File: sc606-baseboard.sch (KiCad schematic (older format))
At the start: 0 parts

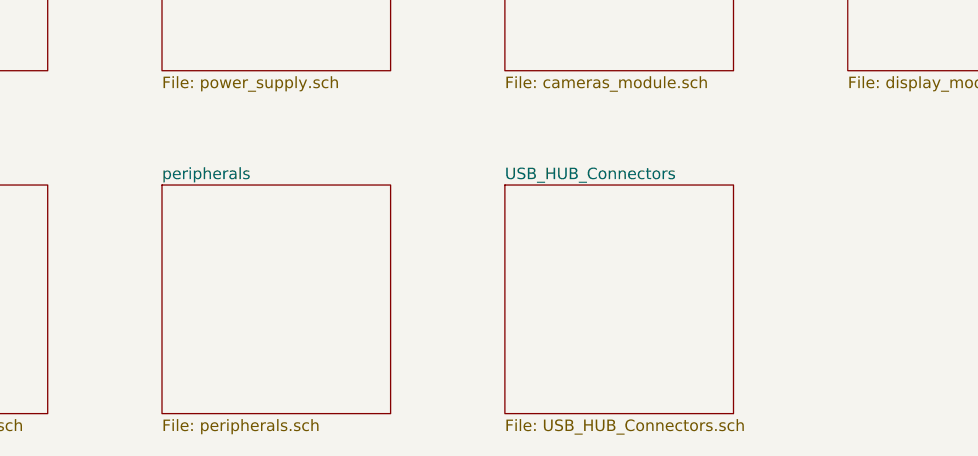
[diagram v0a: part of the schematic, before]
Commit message: Added footprint of 2x USB-A stacked. Added connections to USB HUB.
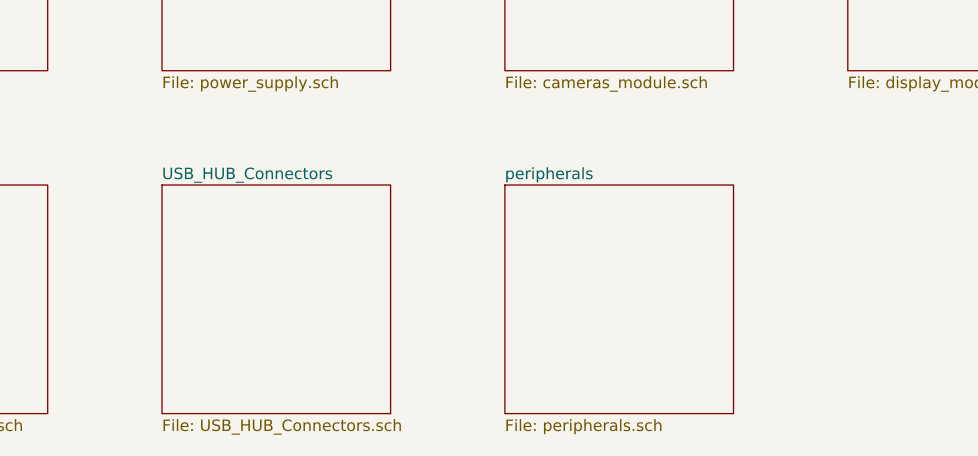
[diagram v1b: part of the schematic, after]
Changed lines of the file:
@@
 $EndSheet
 $Sheet
-S 7000 7500 1000 1000
+S 8500 7500 1000 1000
 U 61D49FDE
 F0 "peripherals" 50
@@
 $EndSheet
 $Sheet
-S 8500 7500 1000 1000
+S 7000 7500 1000 1000
 U 63348E64
 F0 "USB_HUB_Connectors" 50

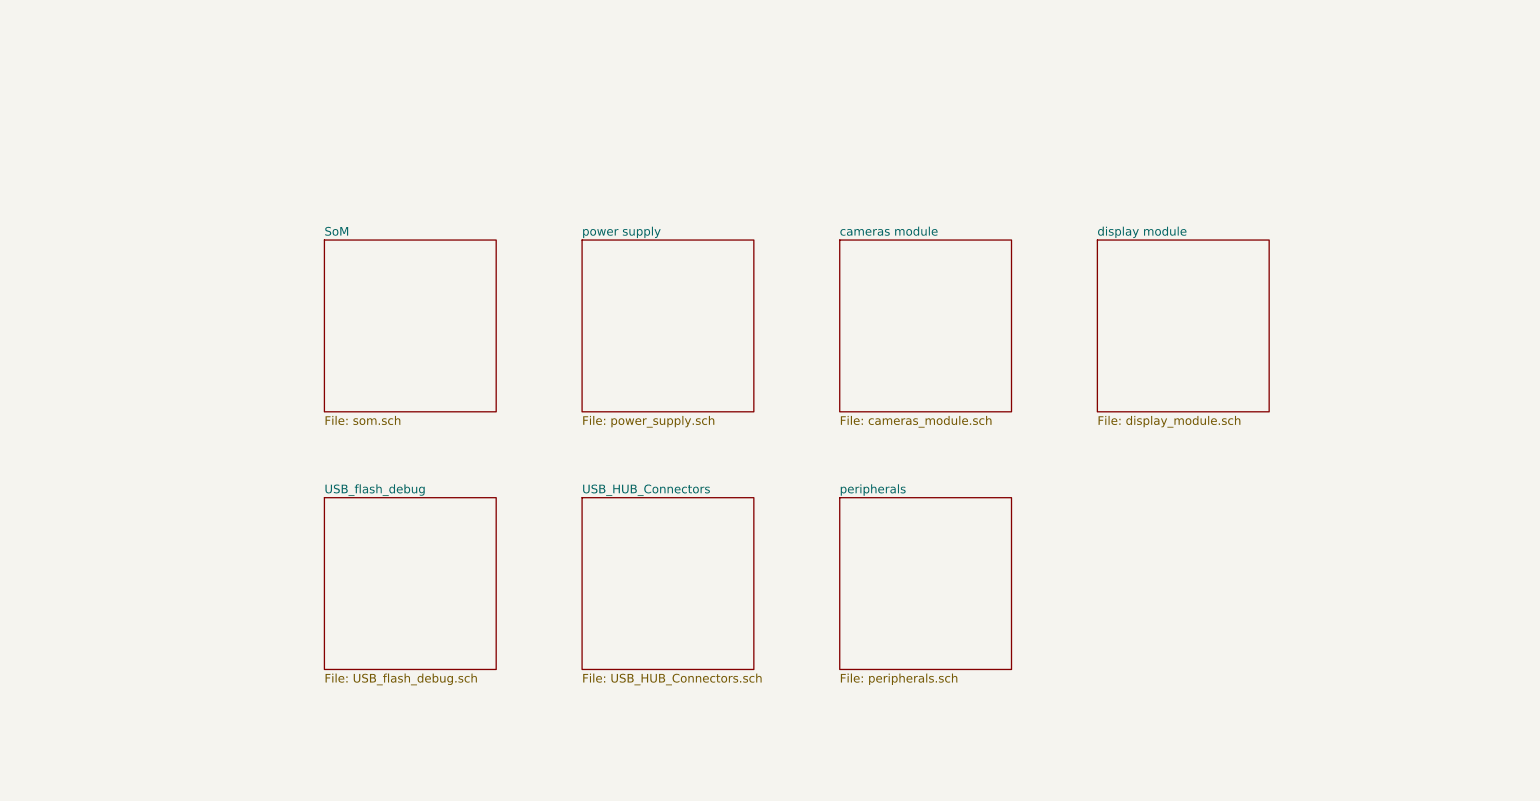
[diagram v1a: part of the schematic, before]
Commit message: Started placing main components on PCB. Change of RT battery model and USB flash connector
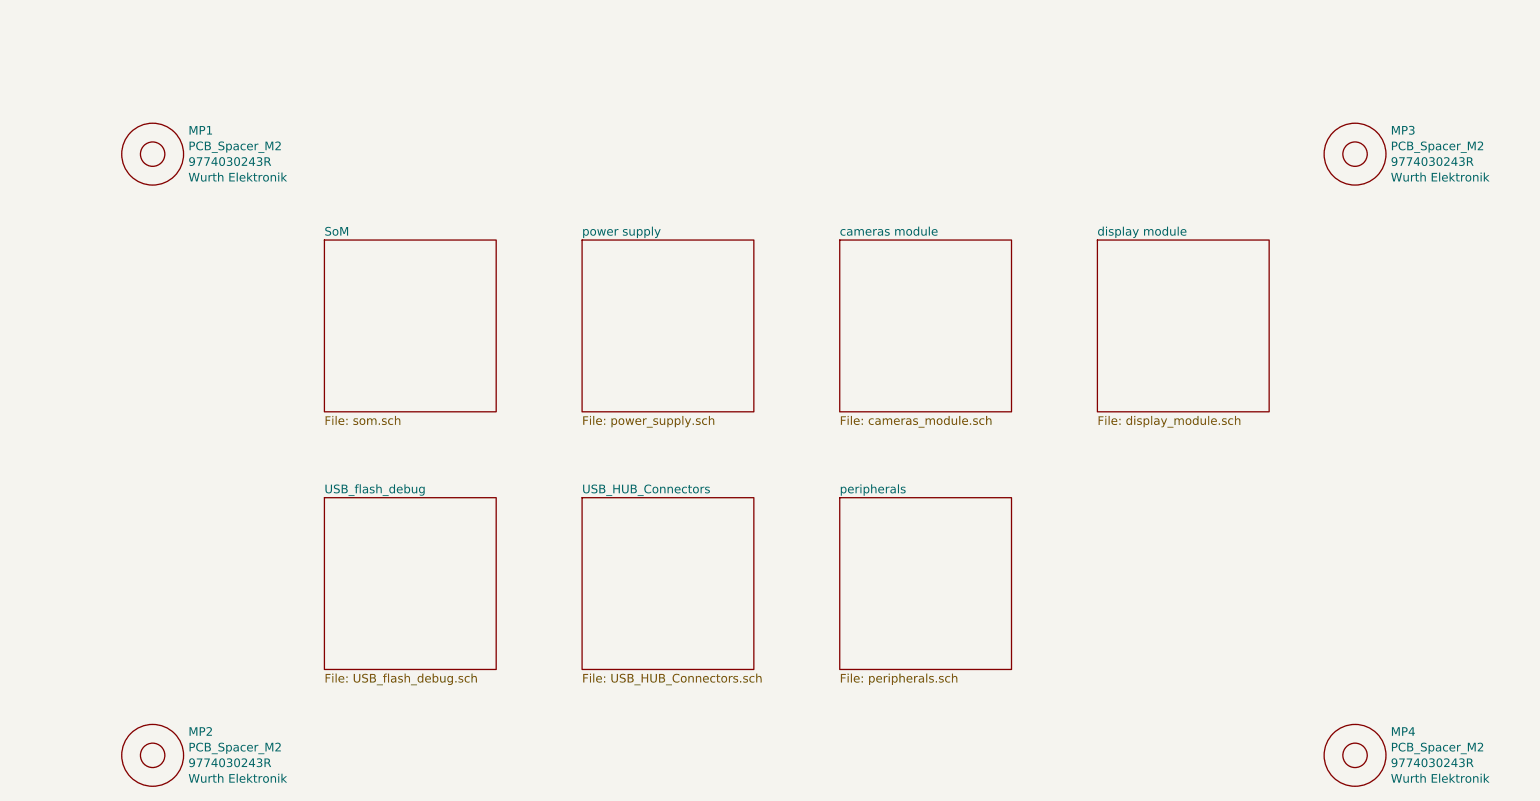
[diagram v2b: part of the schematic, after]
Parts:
- added MP1, MP2, MP3, MP4: PCB_Spacer_M2, sc606-baseboard-footprints:9774030243R, symbol sc606-baseboard:PCB_Spacer_M2
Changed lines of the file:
@@
 F1 "USB_HUB_Connectors.sch" 50
 $EndSheet
+$Comp
+L sc606-baseboard:PCB_Spacer_M2 MP1
+U 1 1 61EAB25E
+P 4500 5500
+F 0 "MP1" H 4708 5637 50  0000 L CNN
+F 1 "PCB_Spacer_M2" H 4708 5546 50  0000 L CNN
+F 2 "sc606-baseboard-footprints:9774030243R" H 5300 6200 50  0001 C CNN
+F 3 "https://katalog.we-online.de/em/datasheet/9774030243R.pdf" H 5450 6300 50  0001 C CNN
+F 4 "9774030243R" H 4708 5455 50  0000 L CNN "MPN"
+F 5 "Wurth Elektronik " H 4708 5364 50  0000 L CNN "Manufacturer"
+	1    4500 5500
+	1    0    0    -1
+$EndComp
+$Comp
+L sc606-baseboard:PCB_Spacer_M2 MP2
+U 1 1 61EAB616
+P 4500 9000
+F 0 "MP2" H 4708 9137 50  0000 L CNN
+F 1 "PCB_Spacer_M2" H 4708 9046 50  0000 L CNN
+F 2 "sc606-baseboard-footprints:9774030243R" H 5300 9700 50  0001 C CNN
+F 3 "https://katalog.we-online.de/em/datasheet/9774030243R.pdf" H 5450 9800 50  0001 C CNN
+F 4 "9774030243R" H 4708 8955 50  0000 L CNN "MPN"
+F 5 "Wurth Elektronik " H 4708 8864 50  0000 L CNN "Manufacturer"
+	1    4500 9000
+	1    0    0    -1
+$EndComp
+$Comp
+L sc606-baseboard:PCB_Spacer_M2 MP4
+U 1 1 61EABD8A
+P 11500 9000
+F 0 "MP4" H 11708 9137 50  0000 L CNN
+F 1 "PCB_Spacer_M2" H 11708 9046 50  0000 L CNN
+F 2 "sc606-baseboard-footprints:9774030243R" H 12300 9700 50  0001 C CNN
+F 3 "https://katalog.we-online.de/em/datasheet/9774030243R.pdf" H 12450 9800 50  0001 C CNN
+F 4 "9774030243R" H 11708 8955 50  0000 L CNN "MPN"
+F 5 "Wurth Elektronik " H 11708 8864 50  0000 L CNN "Manufacturer"
+	1    11500 9000
+	1    0    0    -1
+$EndComp
+$Comp
+L sc606-baseboard:PCB_Spacer_M2 MP3
+U 1 1 61EAC3DC
+P 11500 5500
+F 0 "MP3" H 11708 5637 50  0000 L CNN
+F 1 "PCB_Spacer_M2" H 11708 5546 50  0000 L CNN
+F 2 "sc606-baseboard-footprints:9774030243R" H 12300 6200 50  0001 C CNN
+F 3 "https://katalog.we-online.de/em/datasheet/9774030243R.pdf" H 12450 6300 50  0001 C CNN
+F 4 "9774030243R" H 11708 5455 50  0000 L CNN "MPN"
+F 5 "Wurth Elektronik " H 11708 5364 50  0000 L CNN "Manufacturer"
+	1    11500 5500
+	1    0    0    -1
+$EndComp
 $EndSCHEMATC

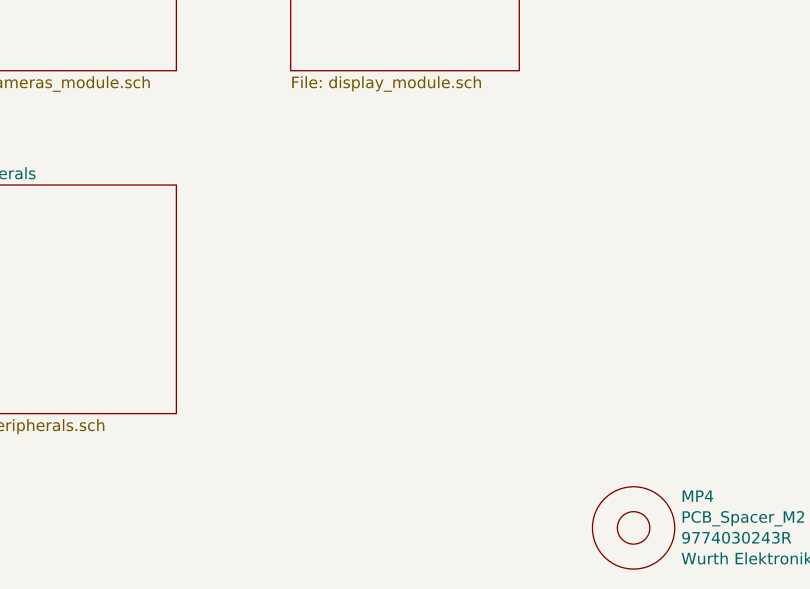
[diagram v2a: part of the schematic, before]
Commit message: Changed USB flash and debug to USB-C. Prepared place for USB PD. Minor modifications of components position
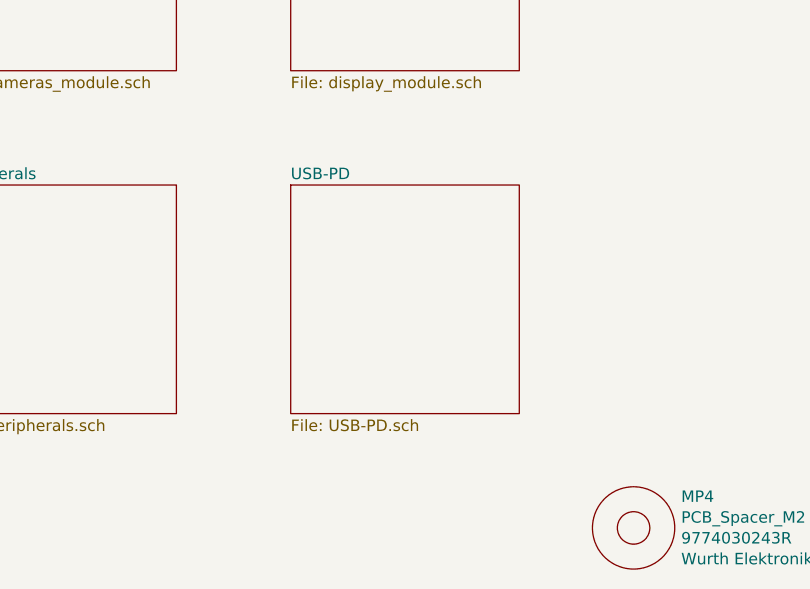
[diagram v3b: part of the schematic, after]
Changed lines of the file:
@@
 $Descr A3 16535 11693
 encoding utf-8
-Sheet 1 8
+Sheet 1 9
 Title ""
 Date "2022-01-04"
@@
 	1    0    0    -1
 $EndComp
+$Sheet
+S 10000 7500 1000 1000
+U 623AED4D
+F0 "USB-PD" 50
+F1 "USB-PD.sch" 50
+$EndSheet
 $EndSCHEMATC

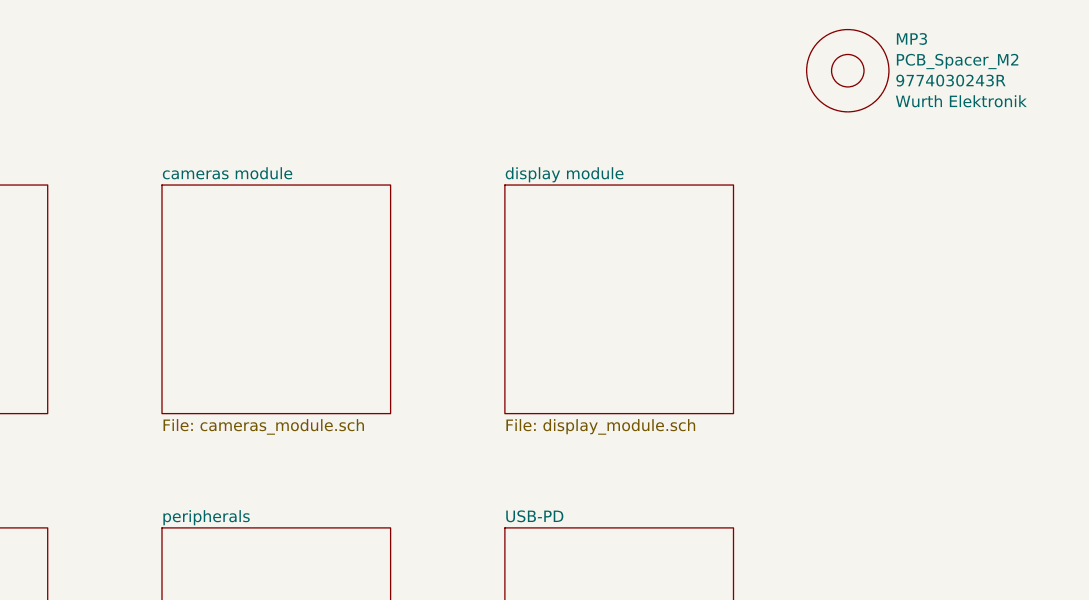
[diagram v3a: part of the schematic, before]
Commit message: Added schema for serial interface connectors
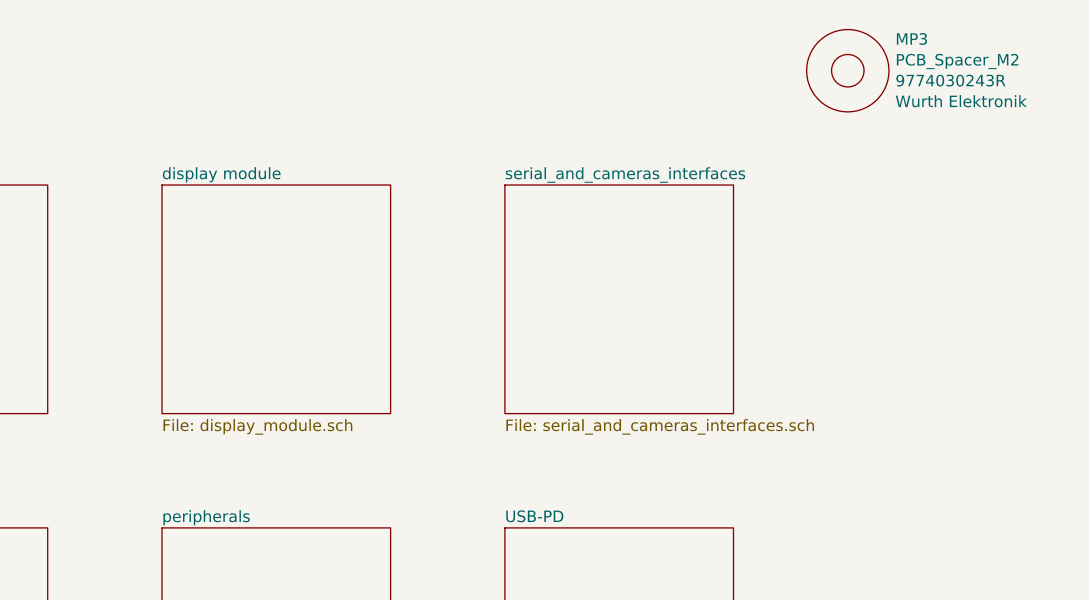
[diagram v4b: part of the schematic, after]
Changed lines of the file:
@@
+$EndSheet
+$Sheet
+S 10000 6000 1000 1000
+U 61D49F95
+F0 "serial_and_cameras_interfaces" 50
+F1 "serial_and_cameras_interfaces.sch" 50
 $EndSheet
 $Sheet
 S 8500 6000 1000 1000
-U 61D49F95
-F0 "cameras module" 50
-F1 "cameras_module.sch" 50
-$EndSheet
-$Sheet
-S 10000 6000 1000 1000
 U 61D49FBF
 F0 "display module" 50

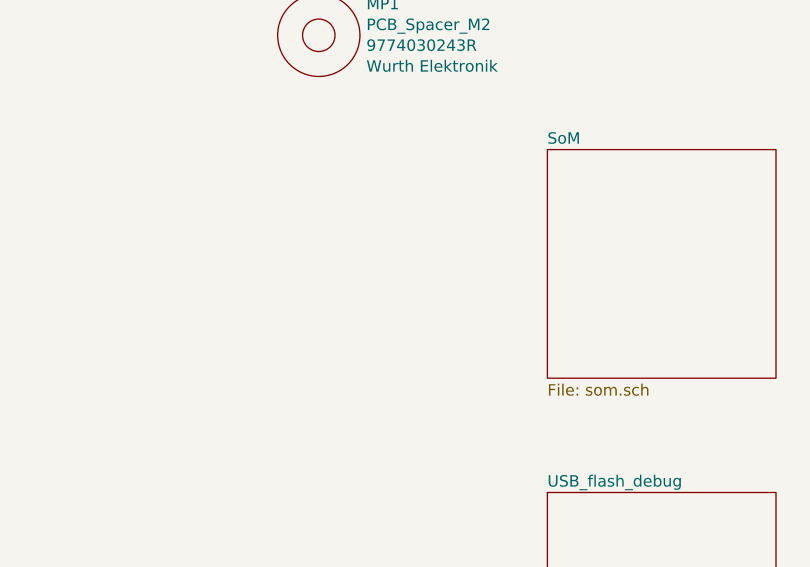
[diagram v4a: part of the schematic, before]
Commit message: Corrected errors from feedback. Added board name, version, Antmicro and OSHW logo, connector labels, button and LED descriptions
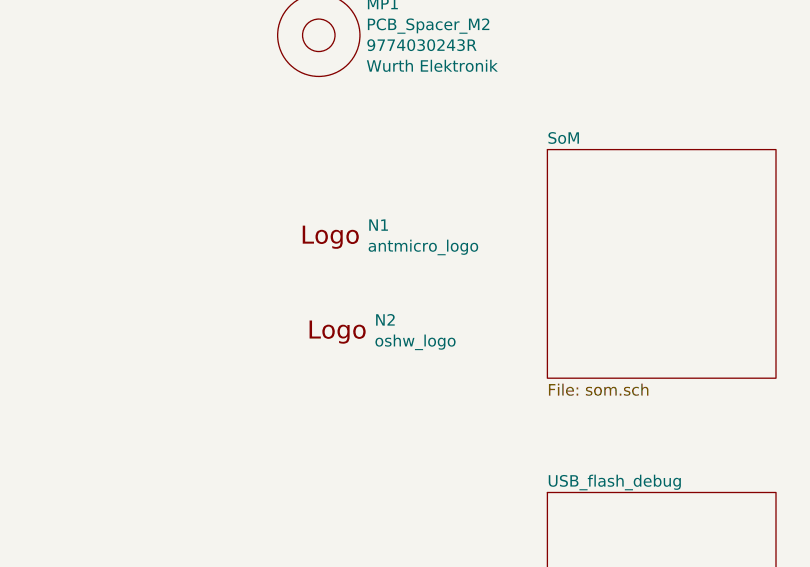
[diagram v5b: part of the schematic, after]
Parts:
- added N1: antmicro_logo, antmicro-footprints:antmicro-logo_scaled_12mm, symbol antmicroMechanicalParts:antmicro_logo
- added N2: oshw_logo, antmicro-footprints:oshw-logo, symbol antmicroMechanicalParts:oshw_logo
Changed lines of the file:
@@
 F1 "USB-PD.sch" 50
 $EndSheet
+$Comp
+L antmicroMechanicalParts:antmicro_logo N1
+U 1 1 620F99C7
+P 4500 6425
+F 0 "N1" H 4714 6518 50  0000 L CNN
+F 1 "antmicro_logo" H 4714 6427 50  0000 L CNN
+F 2 "antmicro-footprints:antmicro-logo_scaled_12mm" H 4400 6675 50  0001 C CNN
+F 3 "" H 4500 6775 50  0001 C CNN
+	1    4500 6425
+	1    0    0    -1
+$EndComp
+$Comp
+L antmicroMechanicalParts:oshw_logo N2
+U 1 1 620FA0FE
+P 4550 6750
+F 0 "N2" H 4744 6753 50  0000 L CNN
+F 1 "oshw_logo" H 4744 6662 50  0000 L CNN
+F 2 "antmicro-footprints:oshw-logo" H 4570 6510 50  0001 C CNN
+F 3 "" H 4550 6750 50  0001 C CNN
+	1    4550 6750
+	1    0    0    -1
+$EndComp
 $EndSCHEMATC

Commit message: Corrected footprint of Q10 and Q11. Used 'kmake loclib'
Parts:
- N1: footprint antmicro-footprints:antmicro-logo_scaled_12mm -> sc606-baseboard-footprints:antmicro-logo_scaled_12mm; symbol antmicroMechanicalParts:antmicro_logo -> sc606-baseboard:antmicro_logo
- N2: footprint antmicro-footprints:oshw-logo -> sc606-baseboard-footprints:oshw-logo; symbol antmicroMechanicalParts:oshw_logo -> sc606-baseboard:oshw_logo
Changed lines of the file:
@@
 $EndSheet
 $Comp
-L antmicroMechanicalParts:antmicro_logo N1
+L sc606-baseboard:antmicro_logo N1
 U 1 1 620F99C7
 P 4500 6425
 F 0 "N1" H 4714 6518 50  0000 L CNN
 F 1 "antmicro_logo" H 4714 6427 50  0000 L CNN
-F 2 "antmicro-footprints:antmicro-logo_scaled_12mm" H 4400 6675 50  0001 C CNN
+F 2 "sc606-baseboard-footprints:antmicro-logo_scaled_12mm" H 4400 6675 50  0001 C CNN
 F 3 "" H 4500 6775 50  0001 C CNN
 	1    4500 6425
@@
 $EndComp
 $Comp
-L antmicroMechanicalParts:oshw_logo N2
+L sc606-baseboard:oshw_logo N2
 U 1 1 620FA0FE
 P 4550 6750
 F 0 "N2" H 4744 6753 50  0000 L CNN
 F 1 "oshw_logo" H 4744 6662 50  0000 L CNN
-F 2 "antmicro-footprints:oshw-logo" H 4570 6510 50  0001 C CNN
+F 2 "sc606-baseboard-footprints:oshw-logo" H 4570 6510 50  0001 C CNN
 F 3 "" H 4550 6750 50  0001 C CNN
 	1    4550 6750
